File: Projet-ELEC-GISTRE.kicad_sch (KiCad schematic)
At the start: 4 parts, among them U1 ESP32-S3-WROOM-1, U2 LD1117S33TR_SOT223

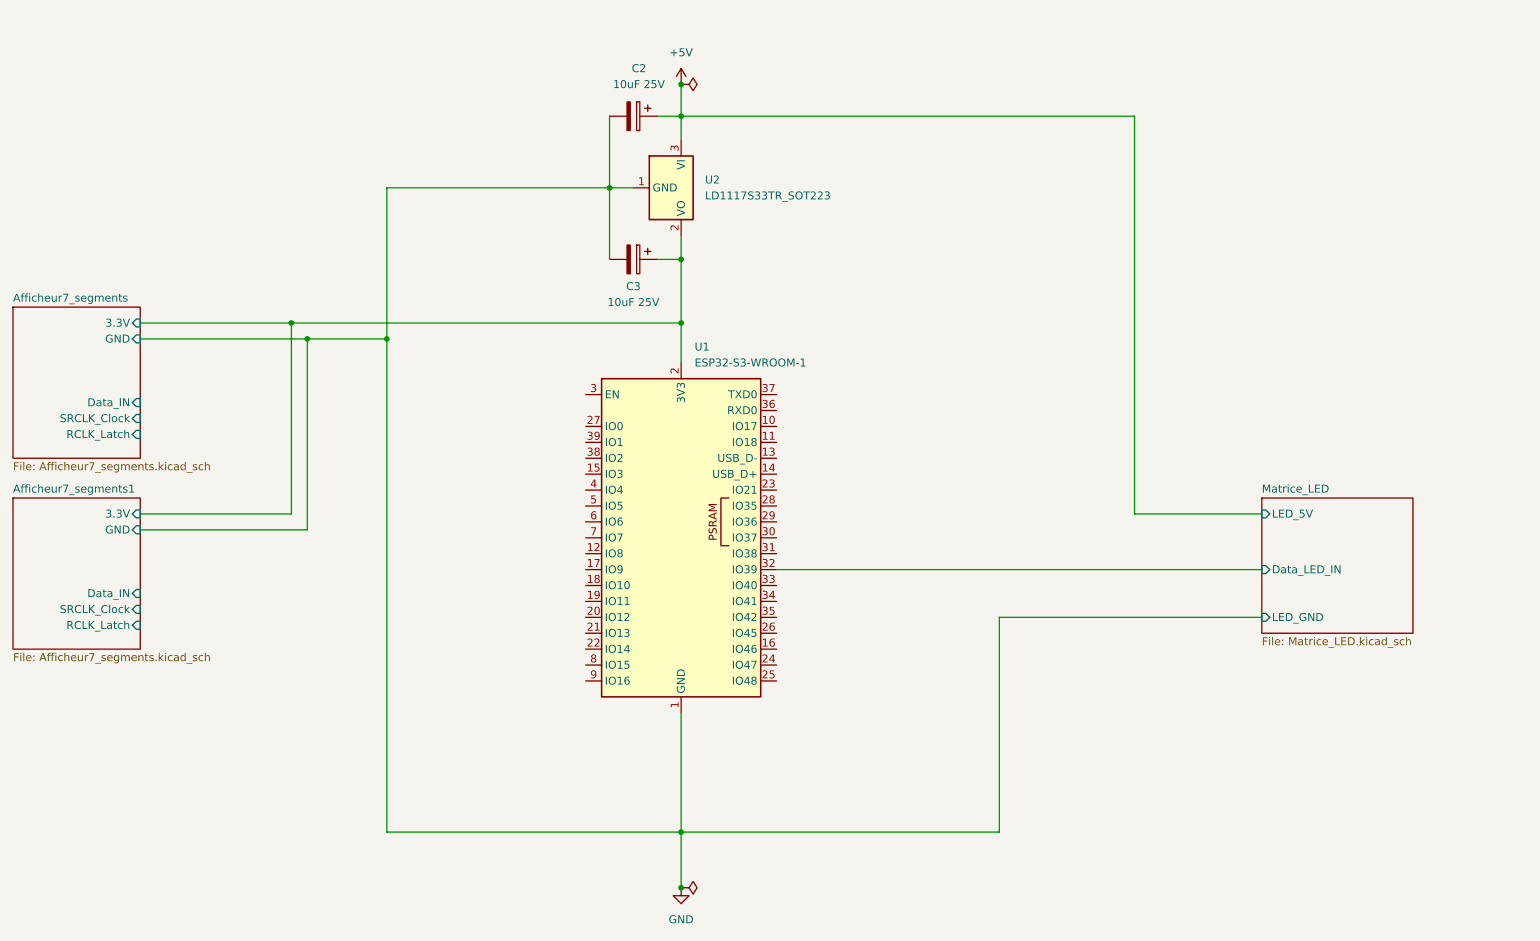
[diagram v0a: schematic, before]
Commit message: Add the barel and the usb to transfer code to esp32
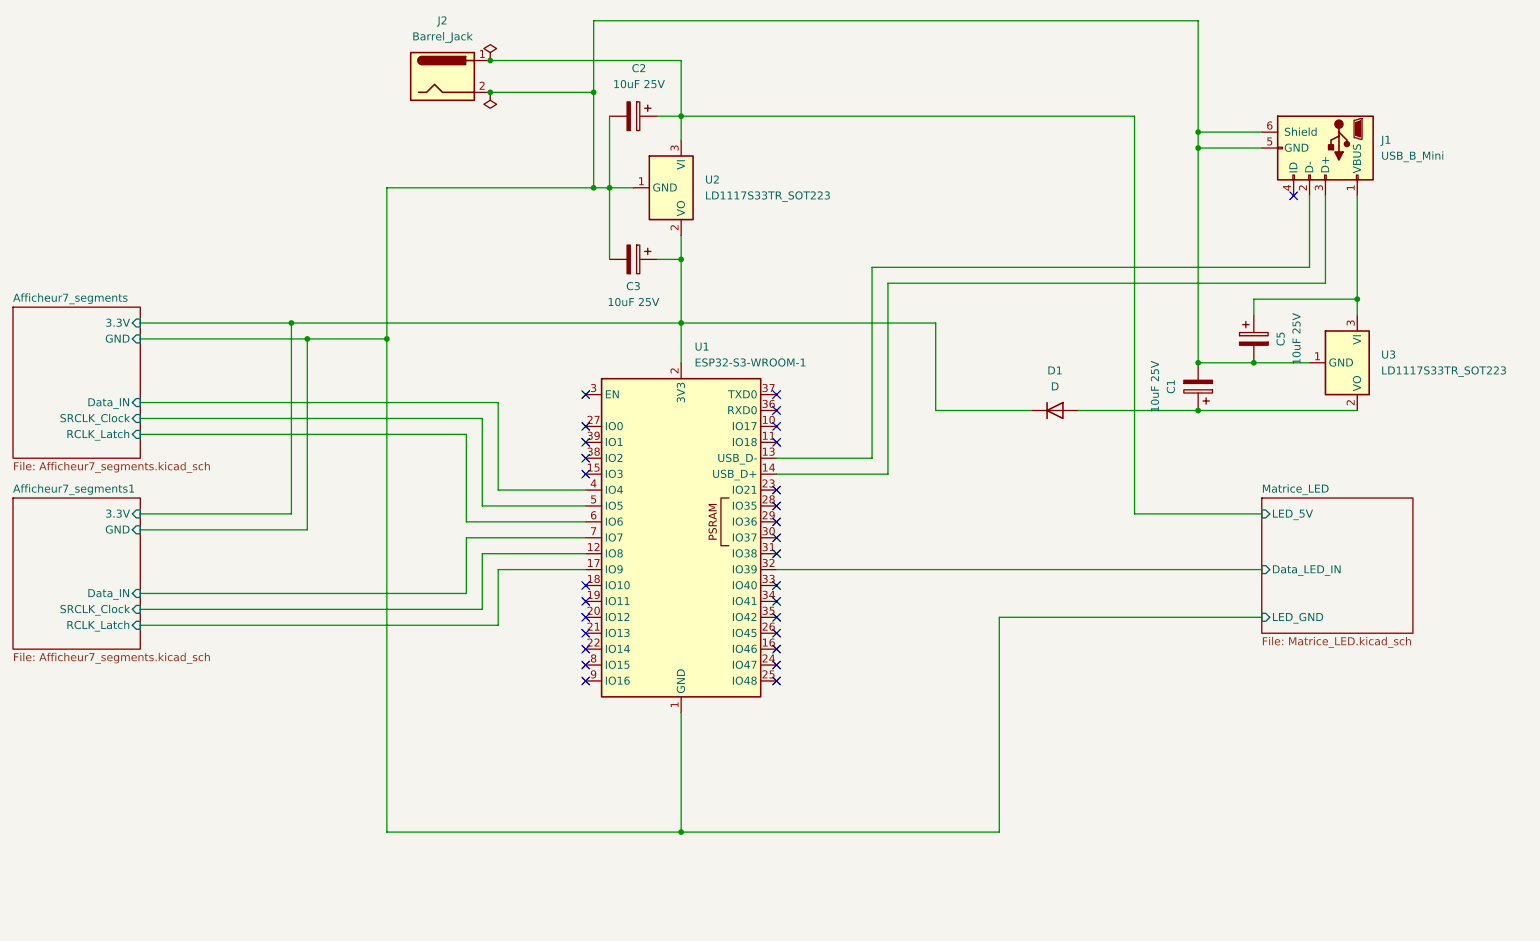
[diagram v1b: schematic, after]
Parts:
- added C1, C5: 10uF 25V, symbol Device:C_Polarized
- added D1: D, symbol Device:D
- added J1: USB_B_Mini, symbol Connector:USB_B_Mini
- added J2: Barrel_Jack, Connector_BarrelJack:BarrelJack_Wuerth_6941xx301002, symbol Connector:Barrel_Jack
- added U3: LD1117S33TR_SOT223, Package_TO_SOT_SMD:SOT-223-3_TabPin2, symbol Regulator_Linear:LD1117S33TR_SOT223
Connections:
- net Afficheur7_segments/3.3V: now also D1.1 (K)
- net Afficheur7_segments/Data_IN: now also U1.4 (IO4)
- net Afficheur7_segments/RCLK_Latch: now also U1.6 (IO6)
- net Afficheur7_segments/SRCLK_Clock: now also U1.5 (IO5)
- net Afficheur7_segments1/Data_IN: now also U1.7 (IO7)
- net Afficheur7_segments1/RCLK_Latch: now also U1.17 (IO9)
- net Afficheur7_segments1/SRCLK_Clock: now also U1.12 (IO8)
- net at U1.13 (USB_D-): now also J1.2 (D-)
- net at U1.14 (USB_D+): now also J1.3 (D+)
- net +5V renamed Matrice_LED/LED_5V
- net Matrice_LED/LED_5V: now also J2.1
- net GND renamed Afficheur7_segments/GND
- net Afficheur7_segments/GND: now also C1.2, C5.2, J1.5 (GND), J1.6 (Shield), J2.2, U3.1 (GND)
- new net: C1.1, D1.2 (A), U3.2 (VO)
- new net: C5.1, J1.1 (VBUS), U3.3 (VI)
- no-connect marks 0 -> 29

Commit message: Save for the review
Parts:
- added D102: SOT23-6L, Package_TO_SOT_SMD:TSOT-23-6_HandSoldering, symbol Device:D
- C1: renamed from C2; footprint (none) -> Capacitor_SMD:C_0603_1608Metric_Pad1.08x0.95mm_HandSolder
- C2: renamed from C3; footprint (none) -> Capacitor_SMD:C_0603_1608Metric_Pad1.08x0.95mm_HandSolder
- C3: renamed from C5; footprint (none) -> Capacitor_SMD:C_0603_1608Metric_Pad1.08x0.95mm_HandSolder
- C4: renamed from C1; footprint (none) -> Capacitor_SMD:C_0603_1608Metric_Pad1.08x0.95mm_HandSolder
- D101: renamed from D1; value D -> SOT23-6L; footprint (none) -> Package_TO_SOT_SMD:TSOT-23-6_HandSoldering
- J1: footprint (none) -> Connector_USB:USB_Mini-B_Wuerth_65100516121_Horizontal
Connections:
- net Afficheur7_segments/3.3V: now also D102.1 (K); no longer C2.1, U2.2 (VO)
- net Afficheur7_segments/Data_IN: now also U1.26 (IO45); no longer U1.4 (IO4)
- net Afficheur7_segments/RCLK_Latch: now also U1.25 (IO48); no longer U1.6 (IO6)
- net Afficheur7_segments/SRCLK_Clock: now also U1.24 (IO47); no longer U1.5 (IO5)
- net Afficheur7_segments1/Data_IN: now also U1.15 (IO3); no longer U1.7 (IO7)
- net Afficheur7_segments1/RCLK_Latch: now also U1.16 (IO46); no longer U1.17 (IO9)
- net Afficheur7_segments1/SRCLK_Clock: now also U1.17 (IO9); no longer U1.12 (IO8)
- net Matrice_LED/Data_LED_IN: now also U1.21 (IO13); no longer U1.32 (IO39)
- new net: C2.1, D102.2 (A), U2.2 (VO)
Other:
- moved on the sheet: C4
